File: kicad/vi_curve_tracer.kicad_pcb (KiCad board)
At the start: 2 copper layers, 60 x 37 mm, 68 parts, among them P1 CONN_01X05, P2 USB_OTG, P3 CONN_01X06, P4 CONN_01X06, P5 CONN_01X02, U1 MCP6004, U2 pic24f08km202, U3 ft230x

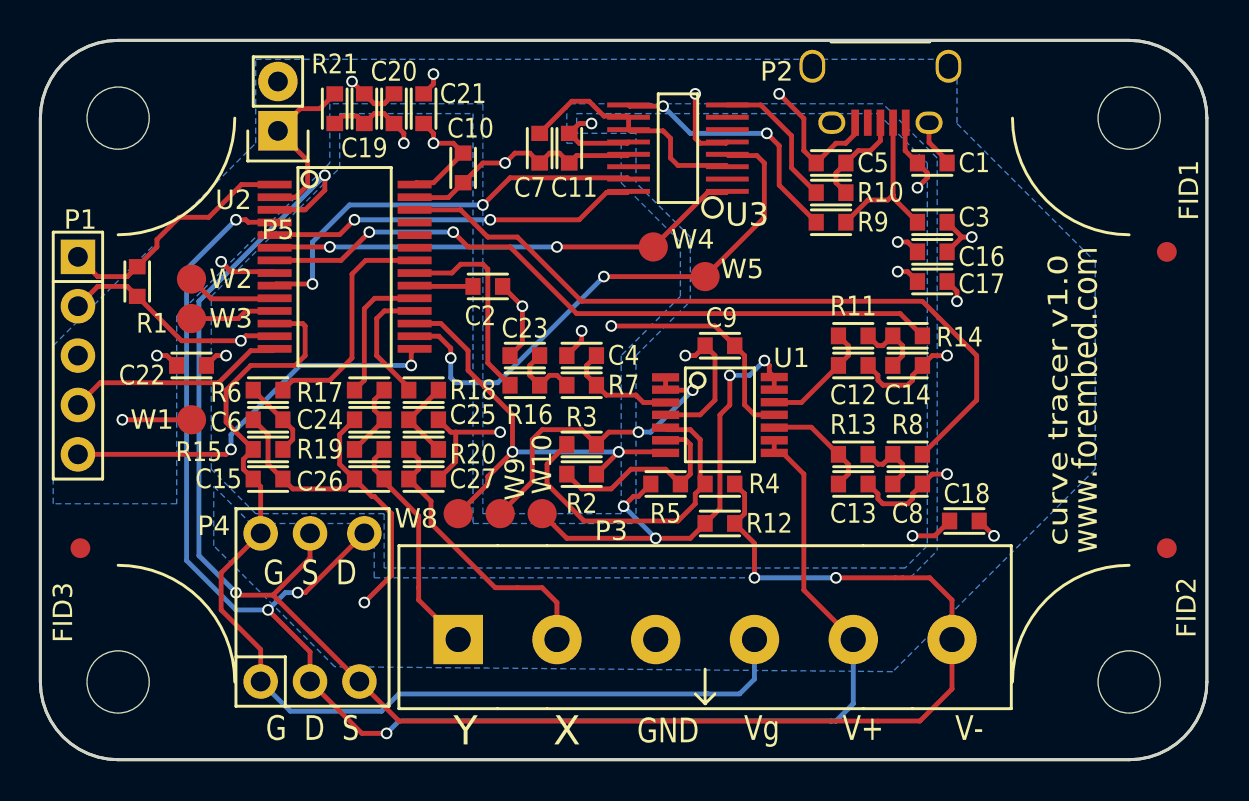
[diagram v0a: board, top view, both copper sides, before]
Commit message: Added safety (multimeter) probes for maximimum compatiblity with likely components that the user already has
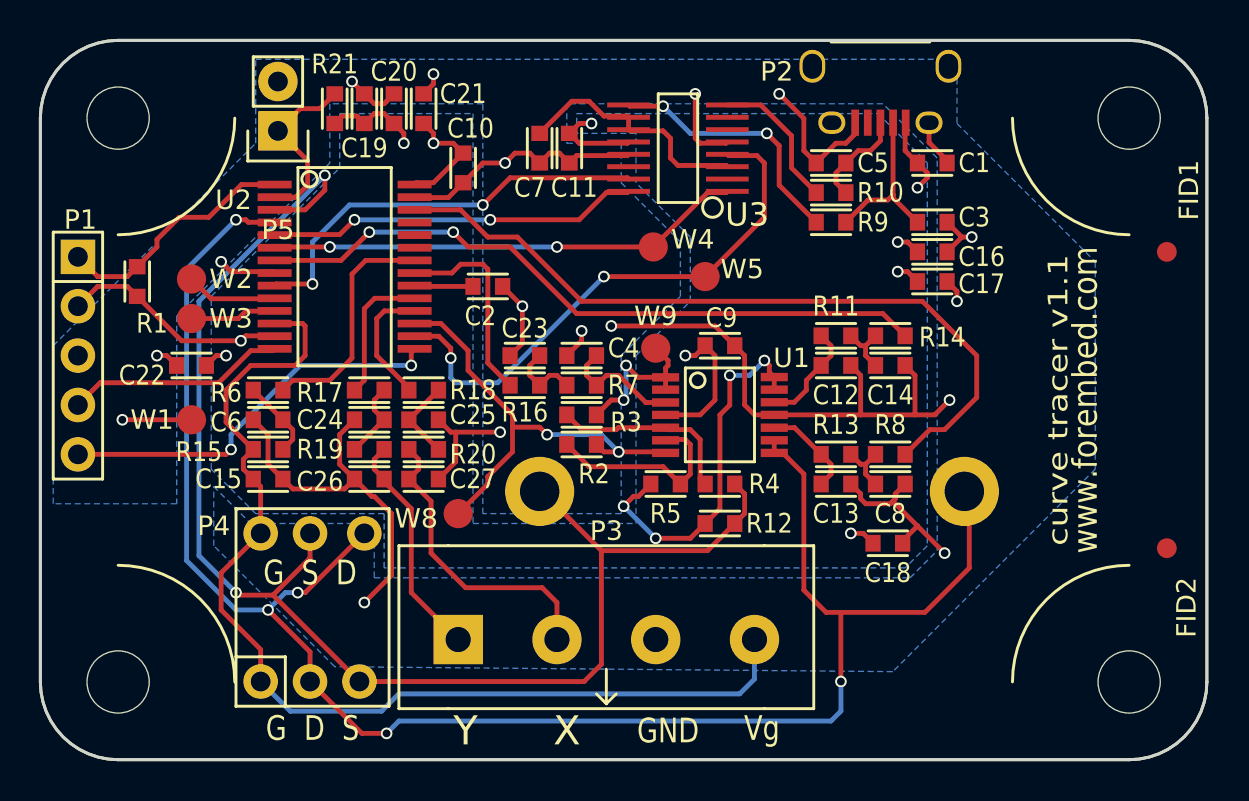
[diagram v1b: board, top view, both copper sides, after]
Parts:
- removed FID3: fiducial, kicad_pcb:fiducial
- removed W10: TEST_1P, Measurement_Points:Measurement_Point_Round-SMD-Pad_Small
- added P6: CONN_01X01, kicad_pcb:CONN_1x1_CT3150, B.Cu at (214.0, 98.4)
- added P7: CONN_01X01, kicad_pcb:CONN_1x1_CT3150, B.Cu at (192.2, 98.4)
- P3: value CONN_01X06 -> CONN_01X04; footprint kicad_pcb:CONN_1x6_OSTTC062162 -> kicad_pcb:CONN_1x4_OSTTC042162
- moved W9 11.7 mm to (198.1, 91.1)
- moved P3 5.08 mm to (195.6, 106.0)
- moved C18 4.10 mm to (210.1, 101.1)
- moved R2 1.52 mm to (194.3, 96.0)
- moved R3 1.52 mm to (194.3, 94.5)
- moved C12 0.89 mm to (207.4, 91.9)
- moved C13 0.89 mm to (207.4, 98.0)
- moved C14 0.89 mm to (210.2, 91.9)
- moved C8 0.89 mm to (210.2, 98.0)
- moved R11 0.89 mm to (207.4, 90.4)
- moved R13 0.89 mm to (207.4, 96.5)
- moved R14 0.89 mm to (210.2, 90.4)
- moved R8 0.89 mm to (210.2, 96.5)
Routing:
- net LD_VOLTAGE_1: track 93.8 -> 72.9 mm, vias 4 -> 2
- net GNDD: track 97.5 -> 109.4 mm, vias 18 -> 17
- net LD_VOLTAGE_0: track 82.2 -> 92.8 mm, vias 4 -> 5
- net /IsenseReference: track 16.5 -> 8.31 mm
- net Net-(R3-Pad1): track 16.9 -> 9.86 mm
- net /-Vout: track 25.4 -> 19.0 mm
- net /x: track 14.8 -> 15.7 mm
- net /DAC_low: track 36.1 -> 35.2 mm
- net Net-(C13-Pad1): track 5.84 -> 4.96 mm
- net +5V: track 44.6 -> 43.7 mm
- net /DAC_high: track 38.3 -> 39.1 mm
- net Net-(C8-Pad1): track 3.64 -> 2.92 mm
- net Net-(C14-Pad1): track 3.64 -> 2.92 mm
- net Net-(C12-Pad1): track 6.04 -> 5.46 mm
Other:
- board text added: "curve tracer v1.1"
- board text removed: "curve tracer v1.0"

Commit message: Minor part movement
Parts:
- moved P2 24.8 mm to (226.3, 93.7), turned to 90 degrees
- moved C7 19.2 mm to (211.1, 77.3), turned to 180 degrees
- moved C1 18.5 mm to (218.3, 99.1)
- moved C11 17.5 mm to (211.1, 79.0), turned to 180 degrees
- moved R9 15.6 mm to (218.3, 95.5)
- moved R10 15.5 mm to (218.3, 93.7)
- moved C5 15.3 mm to (218.3, 91.9)
- moved C3 14.0 mm to (218.3, 97.3), turned to 180 degrees
- moved U3 12.4 mm to (211.2, 83.9), turned to 0 degrees
- moved C17 5.83 mm to (218.1, 88.8)
- moved C16 5.80 mm to (218.1, 87.1)
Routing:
- net +5V: track 43.7 -> 63.2 mm
- net FT230X_24MHZ: track 21.8 -> 37.1 mm
- net FT230X_TX_~SLEEP: track 19.1 -> 32.8 mm
- net FT230X_TX: track 24.5 -> 31.1 mm
- net Net-(R9-Pad1): track 13.3 -> 17.2 mm, vias 2 -> 0
- net Net-(C3-Pad1): track 8.65 -> 5.76 mm
- net FT230X_RX: track 28.3 -> 31.0 mm
- net Net-(R10-Pad1): track 7.41 -> 9.54 mm
- net GNDD: track 109.4 -> 107.6 mm, vias 17 -> 19
- net Net-(C7-Pad1): track 12.7 -> 11.3 mm
- net LD_VOLTAGE_0: track 92.8 -> 92.3 mm, vias 5 -> 6

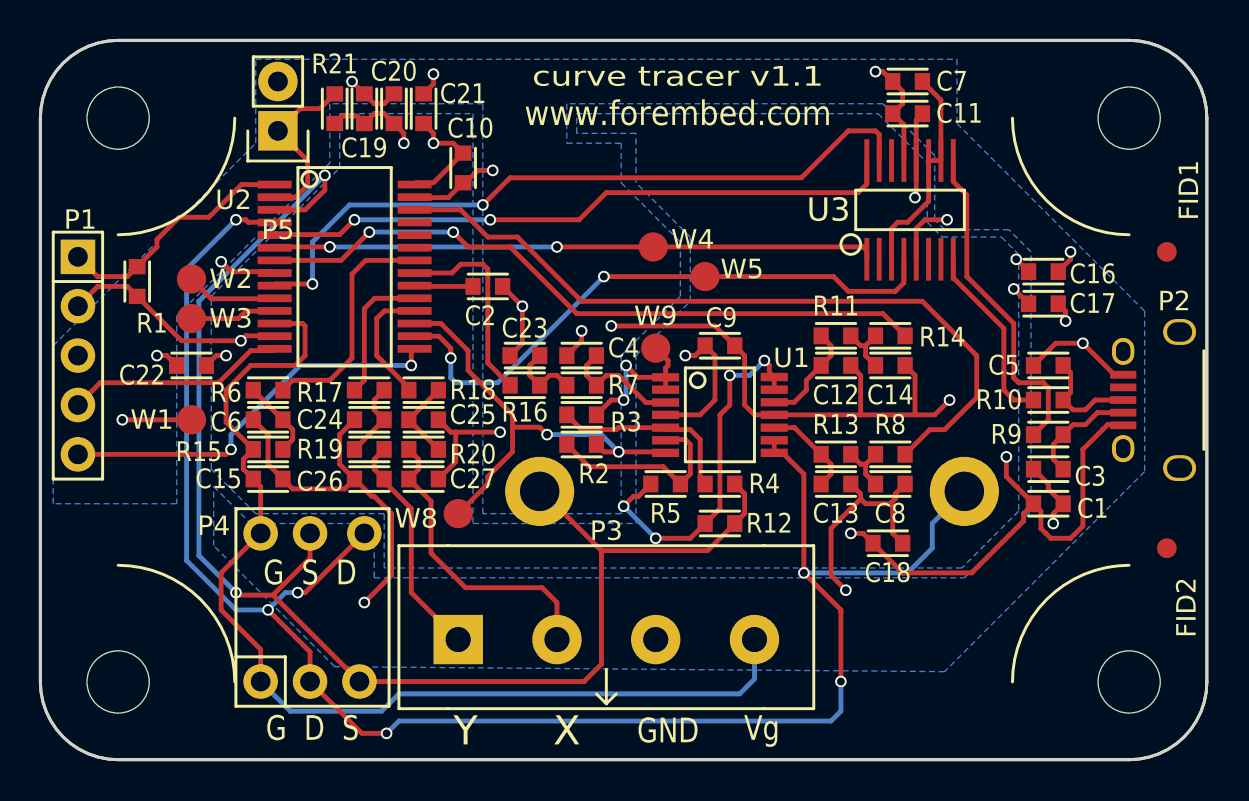
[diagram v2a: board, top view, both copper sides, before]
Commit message: Added features to allow connecting to oscilloscope easier, no change to function.
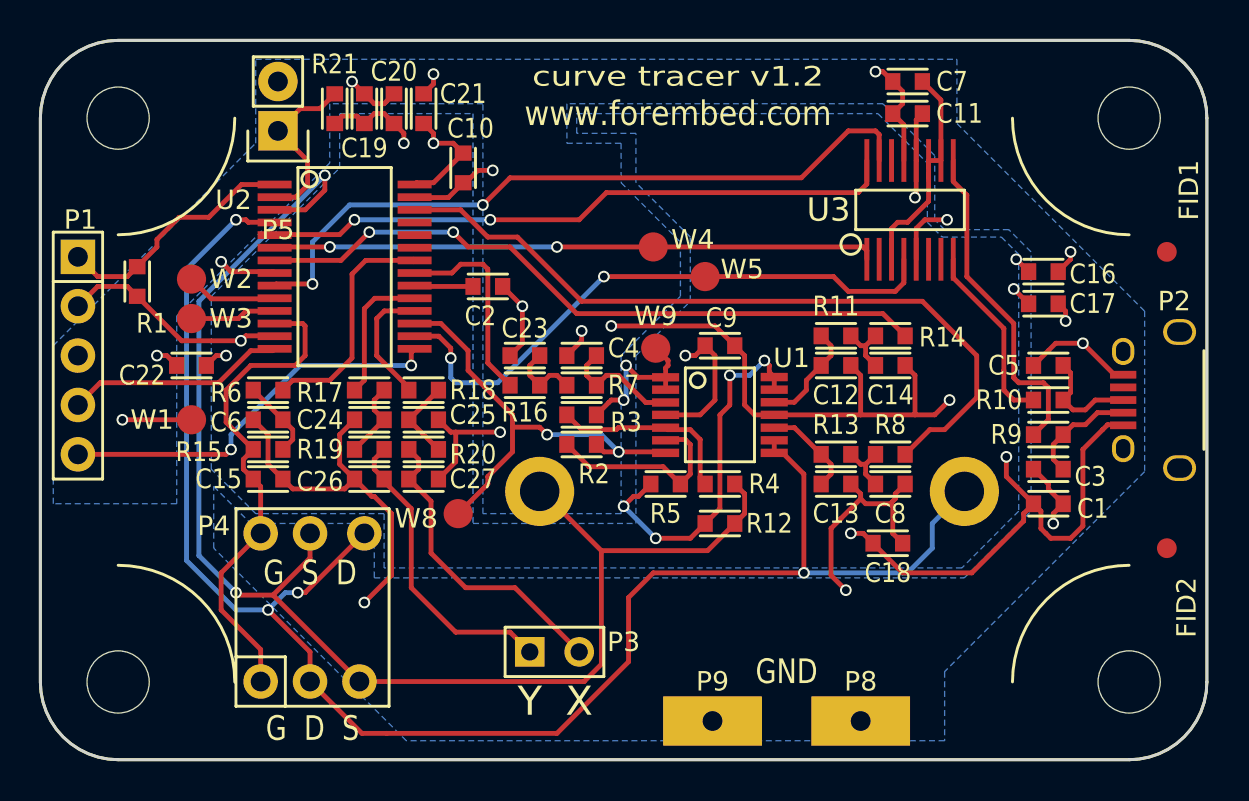
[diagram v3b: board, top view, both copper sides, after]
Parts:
- added P8: CONN_01X01, lib_pcb:CONN_1x1_EDGE_SCOPE_GND, F.Cu at (208.7, 110.2)
- added P9: CONN_01X01, lib_pcb:CONN_1x1_EDGE_SCOPE_GND, F.Cu at (201.0, 110.2)
- P3: value CONN_01X04 -> CONN_01X02; footprint kicad_pcb:CONN_1x4_OSTTC042162 -> lib_pcb:CON_1x2_0.1in
- moved P3 2.74 mm to (192.9, 106.7)
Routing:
- net GateVoltage: track 54.5 -> 25.8 mm
- net LD_VOLTAGE_0: track 92.3 -> 87.3 mm, vias 6 -> 4
- net /y: track 11.8 -> 15.6 mm
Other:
- board text added: "curve tracer v1.2"
- board text removed: "Vg"
- board text removed: "curve tracer v1.1"

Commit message: Moved points to make case design a bit easier
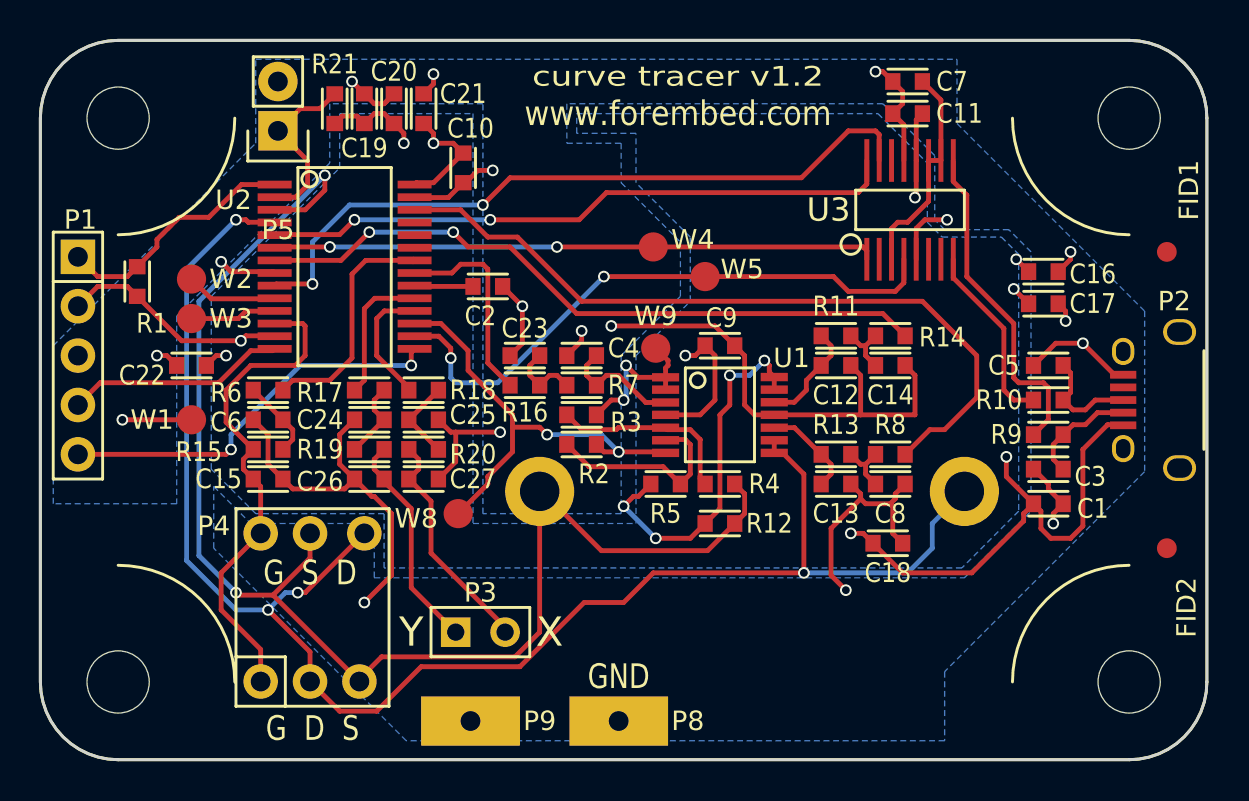
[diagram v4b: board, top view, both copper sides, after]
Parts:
- moved P8 12.4 mm to (196.2, 110.2)
- moved P9 12.4 mm to (188.6, 110.2)
- moved P3 3.94 mm to (189.1, 105.7)
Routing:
- net /y: track 15.6 -> 11.3 mm
- net /x: track 16.0 -> 11.9 mm
- net LD_VOLTAGE_0: track 87.3 -> 84.4 mm
- net GNDD: track 107.6 -> 105.5 mm, vias 19 -> 18
- net LD_VOLTAGE_1: track 72.9 -> 71.9 mm

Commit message: Added fiducial
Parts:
- added FID3: fiducial, kicad_pcb:fiducial, F.Cu at (168.5, 101.3)
